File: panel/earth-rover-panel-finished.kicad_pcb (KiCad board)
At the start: 2 copper layers, 212.1 x 101.6 mm, 127 parts, among them J1 Conn_01x04_Male, J1 Conn_02x04_Male_UnitPerRow, J10 Connector:Screw_Terminal_01x02, J2 Conn_01x04_Male, J3 Conn_01x04_Male, J3 Conn_02x03_Male, J4 Conn_01x04_Male, J4 Conn_02x03_Male, J5 5.4mm/2.5mm, J5 Conn_02x03_Male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

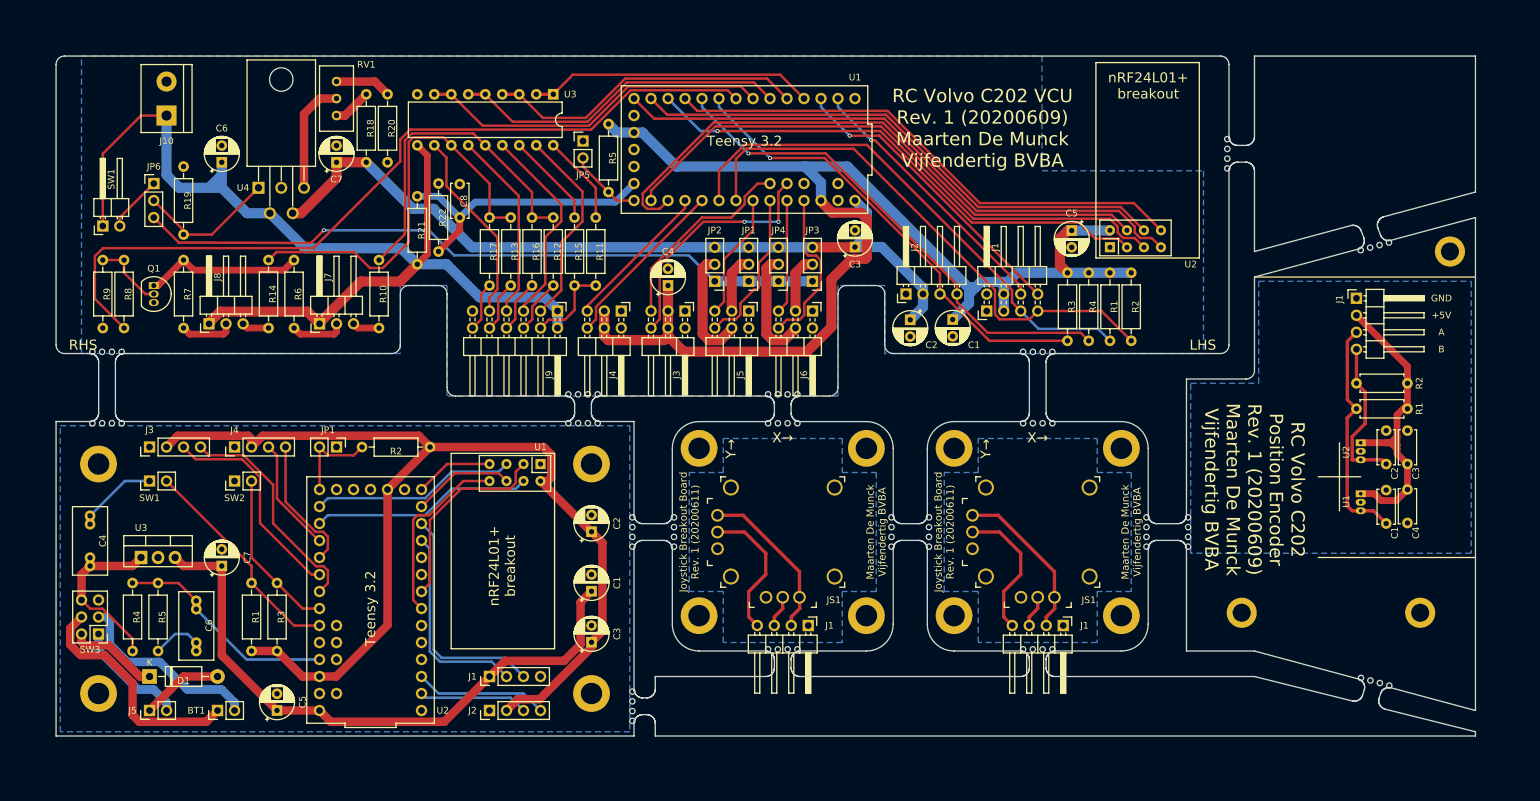
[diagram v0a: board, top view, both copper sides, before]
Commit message: Update panel according to Eurocircuits' specifications
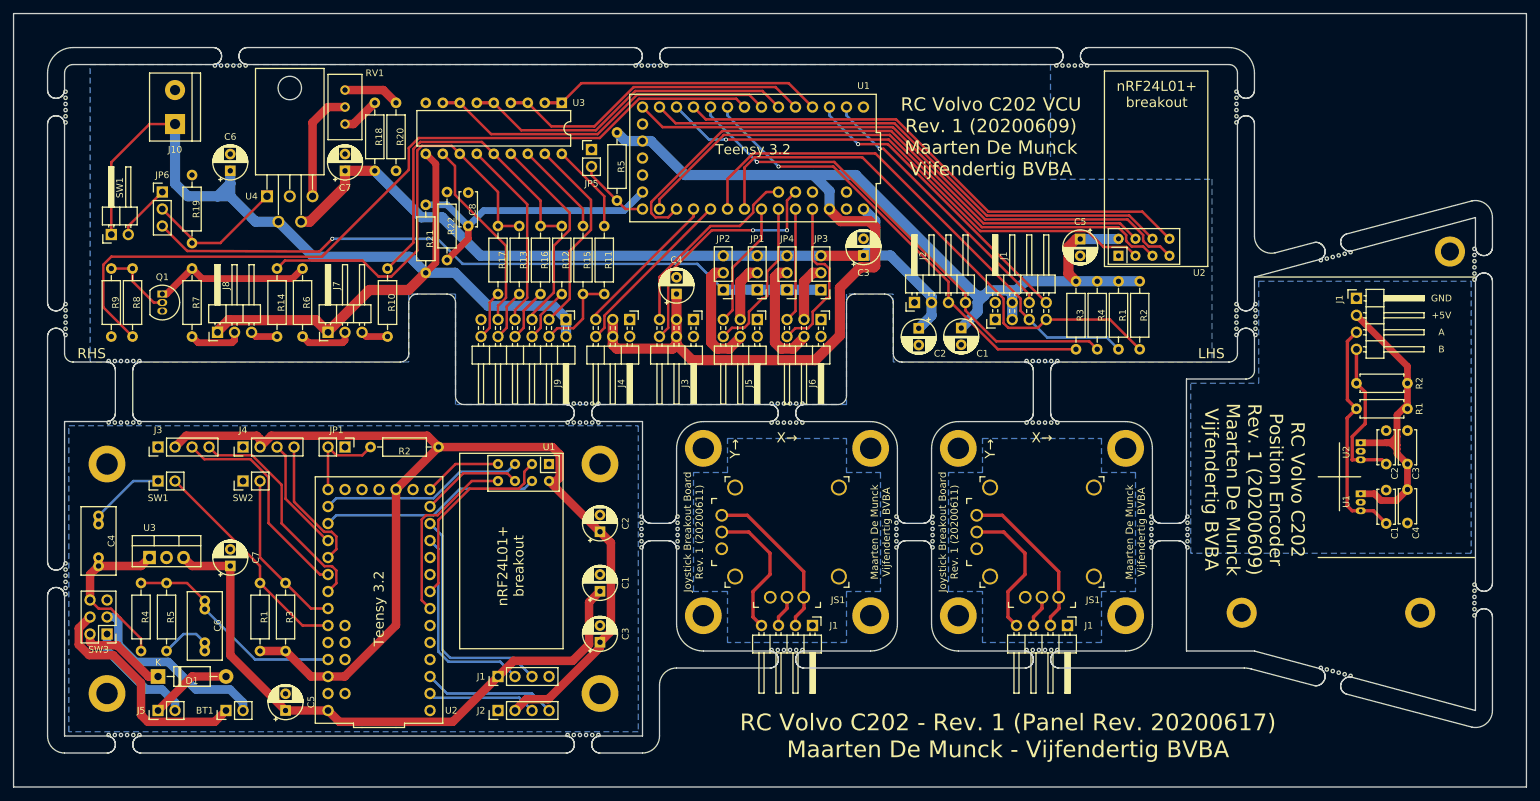
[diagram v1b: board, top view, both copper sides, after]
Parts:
- removed the ? at (220.0, 131.1)
- removed the ? at (278.4, 145.1)
- removed the ? at (253.7, 164.8)
- removed the ? at (215.6, 164.8)
- removed the ? at (234.1, 149.5)
- removed the ? at (239.7, 145.1)
- removed the ? at (201.6, 145.1)
- removed the ? at (195.3, 149.5)
- removed the ? at (190.1, 131.1)
- removed the ? at (185.8, 126.8)
- removed the ? at (119.0, 131.1)
- removed the ? at (215.6, 126.8)
- removed the ? at (114.7, 120.4)
- removed the ? at (258.1, 131.1)
- removed the ? at (253.7, 120.4)
- removed the ? at (195.3, 175.5)
- removed the ? at (284.2, 93.0)
- removed the ? at (304.2, 169.1)
- removed the ? at (308.4, 104.1)
- removed the ? at (272.2, 149.5)
- removed the REF** at (189.2, 137.2)
- removed the REF** at (189.2, 171.4)
- added ?: , holes, F.Cu at (298.2, 167.6)
- added ?: , holes, F.Cu at (321.2, 159.8)
- added ?: , holes, F.Cu at (321.2, 109.6)
- added ?: , holes, F.Cu at (288.4, 113.3)
- added ?: , holes, F.Cu at (285.6, 117.9)
- added ?: , holes, F.Cu at (190.3, 131.0)
- added ?: , holes, F.Cu at (185.7, 128.1)
- added ?: , holes, F.Cu at (121.7, 131.0)
- added ?: , holes, F.Cu at (117.1, 121.8)
- added ?: , holes, F.Cu at (117.1, 177.7)
- added ?: , holes, F.Cu at (185.7, 177.7)
- added ?: , holes, F.Cu at (302.7, 105.5)
- added ?: , holes, F.Cu at (258.8, 131.0)
- added ?: , holes, F.Cu at (254.2, 121.8)
- added ?: , holes, F.Cu at (220.7, 131.0)
- added ?: , holes, F.Cu at (216.1, 128.1)
- added ?: , holes, F.Cu at (202.1, 145.0)
- added ?: , holes, F.Cu at (196.7, 149.6)
- added ?: , holes, F.Cu at (216.1, 164.9)
- added ?: , holes, F.Cu at (254.2, 164.9)
- added ?: , holes, F.Cu at (240.2, 145.0)
- added ?: , holes, F.Cu at (234.8, 149.6)
- added ?: , holes, F.Cu at (110.6, 152.0)
- added ?: , holes, F.Cu at (272.9, 149.6)
- added ?: , holes, F.Cu at (278.3, 145.0)
- added ?: , holes, F.Cu at (200.4, 77.6)
- added ?: , holes, F.Cu at (263.3, 77.6)
- added ?: , holes, F.Cu at (137.6, 77.6)
- added ?: , holes, F.Cu at (110.6, 113.3)
- added ?: , holes, F.Cu at (110.6, 81.5)
- added ?: , holes, F.Cu at (285.6, 86.1)
- added REF**: MountingHole_3.2mm_M3_ISO14580_Pad, MountingHole:MountingHole_3.2mm_M3_ISO14580_Pad, F.Cu at (190.5, 137.2)
- added REF**: MountingHole_3.2mm_M3_ISO14580_Pad, MountingHole:MountingHole_3.2mm_M3_ISO14580_Pad, F.Cu at (190.5, 171.4)
- moved R1 1.80 mm to (268.0, 109.9)
- moved R4 1.80 mm to (264.8, 109.9)
- moved U2 1.80 mm to (268.0, 106.0)
- moved C4 1.80 mm to (201.9, 111.8)
- moved R12 1.80 mm to (184.8, 111.8)
- moved R13 1.80 mm to (178.4, 111.8)
- moved R15 1.80 mm to (188.0, 111.8)
- moved R16 1.80 mm to (181.6, 111.8)
- moved C2 1.80 mm to (238.1, 116.9)
- moved C3 1.80 mm to (229.9, 106.0)
- moved C7 1.80 mm to (152.4, 93.3)
- moved C8 1.80 mm to (170.8, 101.6)
- moved J1 1.80 mm to (249.6, 115.6)
- moved J2 1.80 mm to (237.5, 113.0)
- moved J3 1.80 mm to (204.5, 115.6)
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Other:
- board size 212.1 x 101.6 mm -> 226.1 x 115.6 mm
- board text added: "RC Volvo C202 - Rev. 1 (Panel Rev. 20200617) Maarten De Munck - Vijfendertig BVBA"

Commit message: Use larger holes for nRF24L01+ breakout board
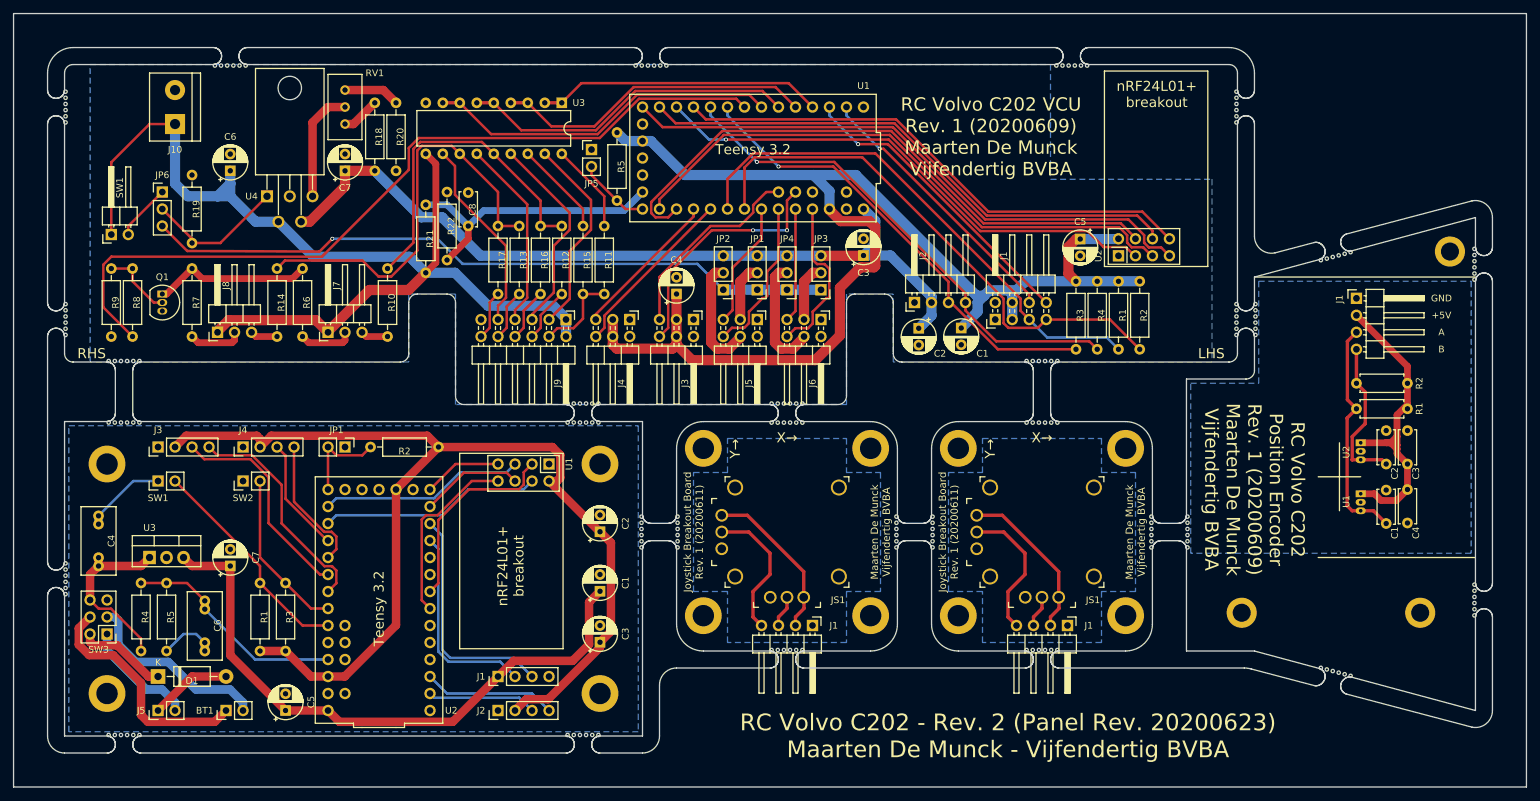
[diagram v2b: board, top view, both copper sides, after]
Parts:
- U1, U2: footprint RF_Module:nRF24L01_Breakout -> earth-rover-footprints:nRF24L01_Breakout_LargerHoles
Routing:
- net /NRF24L01_MOSI: track 97.0 -> 97.8 mm
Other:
- net class Default: clearance 0.25 -> 0.2; trace_width 0.25 -> 0.381
- net class Wide removed
- rule pad_to_mask_clearance: 0.051 -> 0.05
- rule trace_clearance: 0.25 -> 0.2
- board text added: "RC Volvo C202 - Rev. 2 (Panel Rev. 20200623) Maarten De Munck - Vijfendertig BVBA"
- board text removed: "RC Volvo C202 - Rev. 1 (Panel Rev. 20200617) Maarten De Munck - Vijfendertig BVBA"

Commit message: Update panel to KiCad 6.0
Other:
- net class Default removed
